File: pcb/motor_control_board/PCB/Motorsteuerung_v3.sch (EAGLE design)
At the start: 74 parts, among them IC1 TMC5160-TA, IC2 CP2104, J4 10118193-0001LF, Q1 AO4882", Q2 AO4882", Q3 AO4882", Q4 AO4882", Q5 BC817, Q6 BC817, SW1 TL3342F160QG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

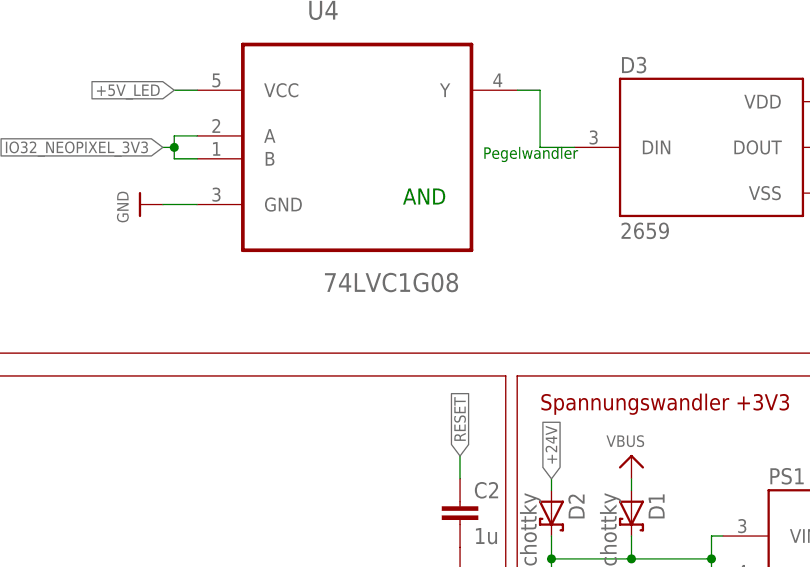
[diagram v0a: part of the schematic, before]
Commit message: Replaced Level Shifter for LEDs. Thanks to Yu-Lien Fang for noticing!
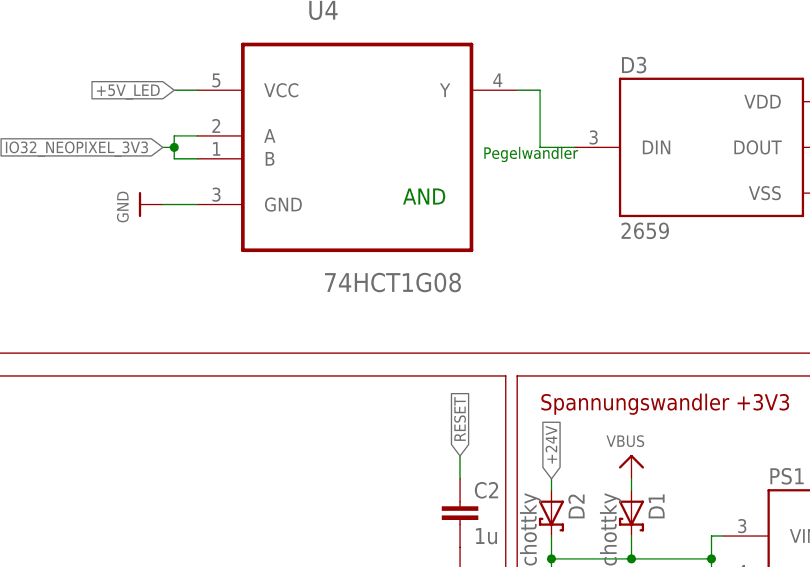
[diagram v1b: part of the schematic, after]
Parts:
- U4: value 74LVC1G08 -> 74HCT1G08
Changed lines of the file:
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@@
 <?xml version="1.0" encoding="utf-8"?>
 <!DOCTYPE eagle SYSTEM "eagle.dtd">
-<eagle version="9.6.0">
+<eagle version="9.6.2">
 <drawing>
 <settings>
@@
 <part name="U$56" library="microbuilder" deviceset="GND" device=""/>
 <part name="C26" library="rcl" library_urn="urn:adsk.eagle:library:334" deviceset="C-EU" device="C0805" package3d_urn="urn:adsk.eagle:package:23617/2" value="100n"/>
-<part name="U4" library="74LVC1G00GW" deviceset="74LVC1G00GW" device="" override_package3d_urn="urn:adsk.eagle:package:21263399/2" override_package_urn="urn:adsk.eagle:footprint:21263400/1" value="74LVC1G08"/>
+<part name="U4" library="74LVC1G00GW" deviceset="74LVC1G00GW" device="" override_package3d_urn="urn:adsk.eagle:package:21263399/2" override_package_urn="urn:adsk.eagle:footprint:21263400/1" value="74HCT1G08"/>
 <part name="U$57" library="microbuilder" deviceset="GND" device=""/>
 <part name="J3" library="SparkFun-Connectors" library_urn="urn:adsk.eagle:library:513" deviceset="CONN_04" device="1.27MM" package3d_urn="urn:adsk.eagle:package:38086/1" override_package3d_urn="urn:adsk.eagle:package:16345249/2" override_package_urn="urn:adsk.eagle:footprint:37705/1"/>
